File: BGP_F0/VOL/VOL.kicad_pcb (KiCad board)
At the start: 2 copper layers, 20 x 26 mm, 2 parts, among them J1 Conn_01x03

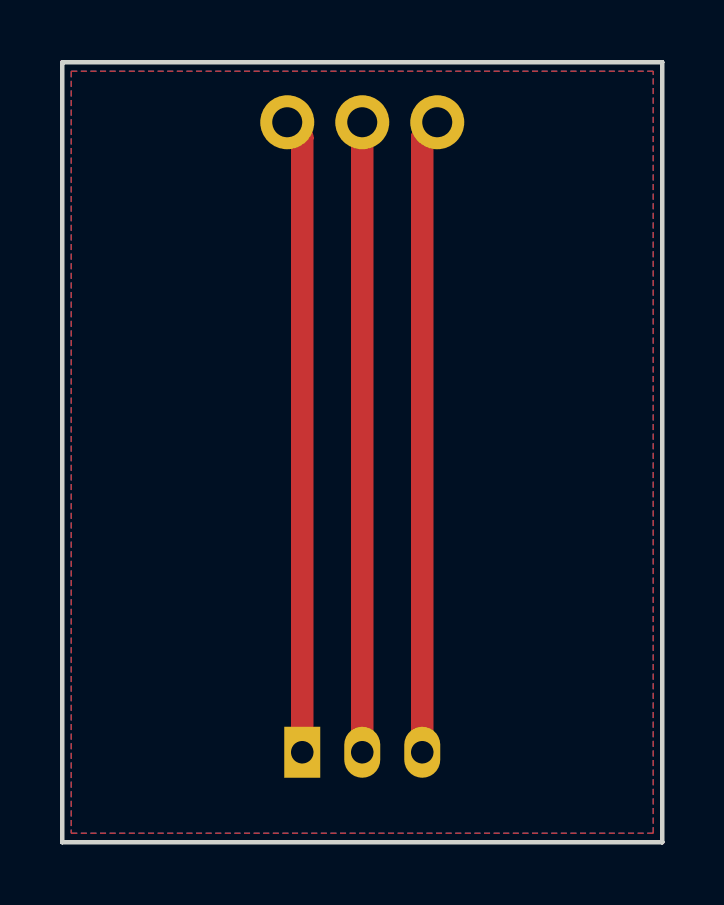
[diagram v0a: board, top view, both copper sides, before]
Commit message: Removed old boards, all F0 are now 26mm deep
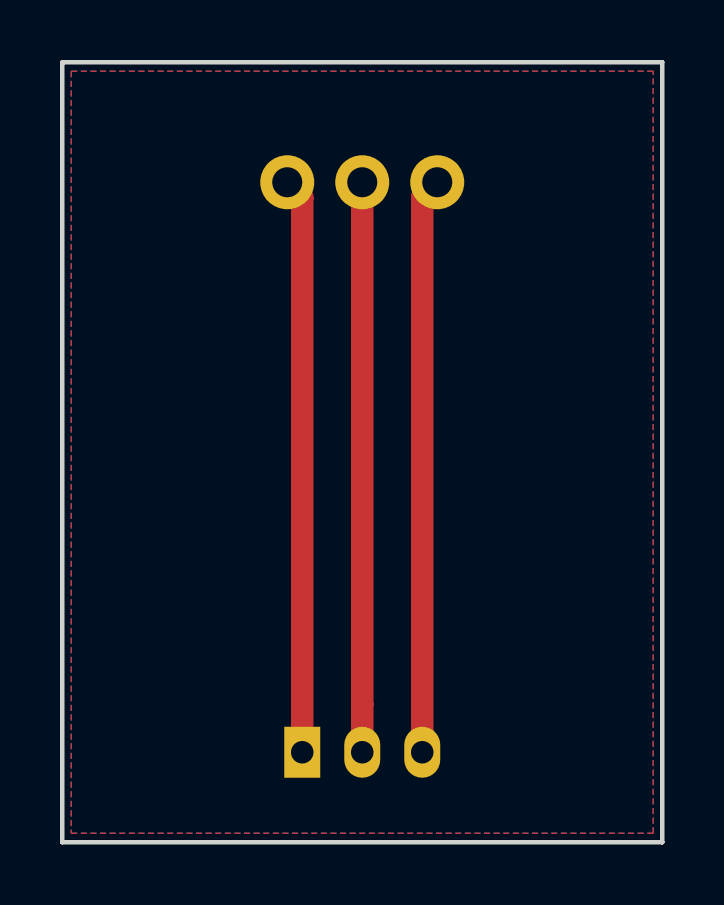
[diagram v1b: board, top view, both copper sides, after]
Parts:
- moved RV1 2.00 mm to (145.5, 80.0)
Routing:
- net /VOL_3: track 21.2 -> 19.2 mm
- net /VOL_2: track 21.0 -> 19.0 mm
- net /VOL_1: track 21.2 -> 19.2 mm
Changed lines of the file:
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@@
-(kicad_pcb (version 4) (host pcbnew 4.0.7)
+(kicad_pcb (version 4) (host pcbnew 4.0.4-1.fc24-product)
   (general
     (links 3)
     (no_connects 0)
-    (area 137.924999 75.924999 158.075001 102.075001)
+    (area 137.924999 75.424999 158.075001 102.075001)
     (thickness 1.6)
     (drawings 8)
-    (tracks 5)
+    (tracks 6)
     (zones 0)
     (modules 2)
@@
     (add_net /VOL_3)
   )
+  (module LIBS:Potentiometer_Alps_RK097_Single_Vertical (layer B.Cu)
+    (at 145.5 80 90)
+    (descr "Potentiometer, vertically mounted, Omeg PC16PU, Omeg PC16PU, Omeg PC16PU, Vishay/Spectrol 248GJ/249GJ Single, Vishay/Spectrol 248GJ/249GJ Single, Vishay/Spectrol 248GJ/249GJ Single, Vishay/Spectrol 248GH/249GH Single, Vishay/Spectrol 148/149 Single, Vishay/Spectrol 148/149 Single, Vishay/Spectrol 148/149 Single, Vishay/Spectrol 148A/149A Single with mounting plates, Vishay/Spectrol 148/149 Double, Vishay/Spectrol 148A/149A Double with mounting plates, Piher PC-16 Single, Piher PC-16 Single, Piher PC-16 Single, Piher PC-16SV Single, Piher PC-16 Double, Piher PC-16 Triple, Piher T16H Single, Piher T16L Single, Piher T16H Double, Alps RK163 Single, Alps RK163 Double, Alps RK097 Single, http://www.alps.com/prod/info/E/HTML/Potentiometer/RotaryPotentiometers/RK097/RK097111080J.html")
+    (tags "Potentiometer vertical  Omeg PC16PU  Omeg PC16PU  Omeg PC16PU  Vishay/Spectrol 248GJ/249GJ Single  Vishay/Spectrol 248GJ/249GJ Single  Vishay/Spectrol 248GJ/249GJ Single  Vishay/Spectrol 248GH/249GH Single  Vishay/Spectrol 148/149 Single  Vishay/Spectrol 148/149 Single  Vishay/Spectrol 148/149 Single  Vishay/Spectrol 148A/149A Single with mounting plates  Vishay/Spectrol 148/149 Double  Vishay/Spectrol 148A/149A Double with mounting plates  Piher PC-16 Single  Piher PC-16 Single  Piher PC-16 Single  Piher PC-16SV Single  Piher PC-16 Double  Piher PC-16 Triple  Piher T16H Single  Piher T16L Single  Piher T16H Double  Alps RK163 Single  Alps RK163 Double  Alps RK097 Single")
+    (fp_text reference RV1 (at 0 7.9 90) (layer B.SilkS)
+      (effects (font (size 0.6 0.6) (thickness 0.15)) (justify mirror))
+    )
+    (fp_text value POT (at 0 -3.5 90) (layer B.Fab) hide
+      (effects (font (size 0.6 0.6) (thickness 0.15)) (justify mirror))
+    )
+    (fp_line (start -2.05 7.25) (end -2.05 -2.25) (layer B.Fab) (width 0.1))
+    (fp_line (start -2.05 -2.25) (end 2 -2.25) (layer B.Fab) (width 0.1))
+    (fp_line (start 2 -2.25) (end 2 7.25) (layer B.Fab) (width 0.1))
+    (fp_line (start 2 7.25) (end -2.05 7.25) (layer B.Fab) (width 0.1))
+    (fp_line (start -2.11 7.31) (end 2.06 7.31) (layer B.SilkS) (width 0.12))
+    (fp_line (start -2.11 -2.31) (end 2.06 -2.31) (layer B.SilkS) (width 0.12))
+    (fp_line (start -2.11 7.31) (end -2.11 -2.31) (layer B.SilkS) (width 0.12))
+    (fp_line (start 2.06 7.31) (end 2.06 -2.31) (layer B.SilkS) (width 0.12))
+    (fp_line (start -2.3 7.5) (end -2.3 -2.5) (layer B.CrtYd) (width 0.05))
+    (fp_line (start -2.3 -2.5) (end 2.25 -2.5) (layer B.CrtYd) (width 0.05))
+    (fp_line (start 2.25 -2.5) (end 2.25 7.5) (layer B.CrtYd) (width 0.05))
+    (fp_line (start 2.25 7.5) (end -2.3 7.5) (layer B.CrtYd) (width 0.05))
+    (pad 3 thru_hole circle (at 0 5 90) (size 1.8 1.8) (drill 1) (layers *.Cu *.Mask)
+      (net 3 /VOL_3))
+    (pad 2 thru_hole circle (at 0 2.5 90) (size 1.8 1.8) (drill 1) (layers *.Cu *.Mask)
+      (net 2 /VOL_2))
+    (pad 1 thru_hole circle (at 0 0 90) (size 1.8 1.8) (drill 1) (layers *.Cu *.Mask)
+      (net 1 /VOL_1))
+    (model Potentiometers.3dshapes/Potentiometer_Alps_RK097_Single_Vertical.wrl
+      (at (xyz 0 0 0))
+      (scale (xyz 0.393701 0.393701 0.393701))
+      (rotate (xyz 0 0 0))
+    )
+  )
   (module Connectors_JST:JST_PH_B3B-PH-K_03x2.00mm_Straight (layer B.Cu)
     (at 146 99)
@@
     )
   )
-  (module LIBS:Potentiometer_Alps_RK097_Single_Vertical (layer B.Cu)
-    (at 145.5 78 90)
-    (descr "Potentiometer, vertically mounted, Omeg PC16PU, Omeg PC16PU, Omeg PC16PU, Vishay/Spectrol 248GJ/249GJ Single, Vishay/Spectrol 248GJ/249GJ Single, Vishay/Spectrol 248GJ/249GJ Single, Vishay/Spectrol 248GH/249GH Single, Vishay/Spectrol 148/149 Single, Vishay/Spectrol 148/149 Single, Vishay/Spectrol 148/149 Single, Vishay/Spectrol 148A/149A Single with mounting plates, Vishay/Spectrol 148/149 Double, Vishay/Spectrol 148A/149A Double with mounting plates, Piher PC-16 Single, Piher PC-16 Single, Piher PC-16 Single, Piher PC-16SV Single, Piher PC-16 Double, Piher PC-16 Triple, Piher T16H Single, Piher T16L Single, Piher T16H Double, Alps RK163 Single, Alps RK163 Double, Alps RK097 Single, http://www.alps.com/prod/info/E/HTML/Potentiometer/RotaryPotentiometers/RK097/RK097111080J.html")
-    (tags "Potentiometer vertical  Omeg PC16PU  Omeg PC16PU  Omeg PC16PU  Vishay/Spectrol 248GJ/249GJ Single  Vishay/Spectrol 248GJ/249GJ Single  Vishay/Spectrol 248GJ/249GJ Single  Vishay/Spectrol 248GH/249GH Single  Vishay/Spectrol 148/149 Single  Vishay/Spectrol 148/149 Single  Vishay/Spectrol 148/149 Single  Vishay/Spectrol 148A/149A Single with mounting plates  Vishay/Spectrol 148/149 Double  Vishay/Spectrol 148A/149A Double with mounting plates  Piher PC-16 Single  Piher PC-16 Single  Piher PC-16 Single  Piher PC-16SV Single  Piher PC-16 Double  Piher PC-16 Triple  Piher T16H Single  Piher T16L Single  Piher T16H Double  Alps RK163 Single  Alps RK163 Double  Alps RK097 Single")
-    (fp_text reference RV1 (at 0 7.9 90) (layer B.SilkS)
-      (effects (font (size 0.6 0.6) (thickness 0.15)) (justify mirror))
-    )
-    (fp_text value POT (at 0 -3.5 90) (layer B.Fab) hide
-      (effects (font (size 0.6 0.6) (thickness 0.15)) (justify mirror))
-    )
-    (fp_line (start -2.05 7.25) (end -2.05 -2.25) (layer B.Fab) (width 0.1))
-    (fp_line (start -2.05 -2.25) (end 2 -2.25) (layer B.Fab) (width 0.1))
-    (fp_line (start 2 -2.25) (end 2 7.25) (layer B.Fab) (width 0.1))
-    (fp_line (start 2 7.25) (end -2.05 7.25) (layer B.Fab) (width 0.1))
-    (fp_line (start -2.11 7.31) (end 2.06 7.31) (layer B.SilkS) (width 0.12))
-    (fp_line (start -2.11 -2.31) (end 2.06 -2.31) (layer B.SilkS) (width 0.12))
-    (fp_line (start -2.11 7.31) (end -2.11 -2.31) (layer B.SilkS) (width 0.12))
-    (fp_line (start 2.06 7.31) (end 2.06 -2.31) (layer B.SilkS) (width 0.12))
-    (fp_line (start -2.3 7.5) (end -2.3 -2.5) (layer B.CrtYd) (width 0.05))
-    (fp_line (start -2.3 -2.5) (end 2.25 -2.5) (layer B.CrtYd) (width 0.05))
-    (fp_line (start 2.25 -2.5) (end 2.25 7.5) (layer B.CrtYd) (width 0.05))
-    (fp_line (start 2.25 7.5) (end -2.3 7.5) (layer B.CrtYd) (width 0.05))
-    (pad 3 thru_hole circle (at 0 5 90) (size 1.8 1.8) (drill 1) (layers *.Cu *.Mask)
-      (net 3 /VOL_3))
-    (pad 2 thru_hole circle (at 0 2.5 90) (size 1.8 1.8) (drill 1) (layers *.Cu *.Mask)
-      (net 2 /VOL_2))
-    (pad 1 thru_hole circle (at 0 0 90) (size 1.8 1.8) (drill 1) (layers *.Cu *.Mask)
-      (net 1 /VOL_1))
-    (model Potentiometers.3dshapes/Potentiometer_Alps_RK097_Single_Vertical.wrl
-      (at (xyz 0 0 0))
-      (scale (xyz 0.393701 0.393701 0.393701))
-      (rotate (xyz 0 0 0))
-    )
-  )
   (gr_line (start 157.7 101.7) (end 157.7 76.3) (layer Margin) (width 0.2))
   (gr_line (start 138.3 101.7) (end 157.7 101.7) (layer Margin) (width 0.2))
@@
   (gr_line (start 138 76) (end 138 102) (layer Edge.Cuts) (width 0.15))
   (gr_line (start 158 76) (end 138 76) (layer Edge.Cuts) (width 0.15))
-  (segment (start 146 99) (end 146 78.5) (width 0.75) (layer F.Cu) (net 1))
-  (segment (start 146 78.5) (end 145.5 78) (width 0.75) (layer F.Cu) (net 1))
-  (segment (start 148 99) (end 148 78) (width 0.75) (layer F.Cu) (net 2))
-  (segment (start 150 99) (end 150 78.5) (width 0.75) (layer F.Cu) (net 3))
-  (segment (start 150 78.5) (end 150.5 78) (width 0.75) (layer F.Cu) (net 3))
+  (segment (start 146 99) (end 146 80.5) (width 0.75) (layer F.Cu) (net 1))
+  (segment (start 146 80.5) (end 145.5 80) (width 0.75) (layer F.Cu) (net 1))
+  (segment (start 148 99) (end 148 97.4) (width 0.75) (layer F.Cu) (net 2))
+  (segment (start 148 97.4) (end 148 80) (width 0.75) (layer F.Cu) (net 2))
+  (segment (start 150 99) (end 150 80.5) (width 0.75) (layer F.Cu) (net 3))
+  (segment (start 150 80.5) (end 150.5 80) (width 0.75) (layer F.Cu) (net 3))
   (zone (net 0) (net_name "") (layer B.Cu) (hatch edge 0.508)
     (connect_pads (clearance 0.3))

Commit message: F0 Final
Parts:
- removed J1: Conn_01x03, Connectors_JST:JST_PH_B3B-PH-K_03x2.00mm_Straight
- added C1: 47n, Capacitors_SMD:C_1206, F.Cu at (150.6, 89.1)
- added P1: CONN_01X02, Connectors_JST:JST_PH_B2B-PH-K_02x2.00mm_Straight, B.Cu at (147.0, 98.5)
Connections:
- RV1 pad 2: /VOL_2 -> /VOL_1
- RV1 pad 3: /VOL_3 -> Net-(C1-Pad1)
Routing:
- net /VOL_2: track 19.0 -> 0.00 mm
- net /VOL_3: track 19.2 -> 8.56 mm
- net Net-(C1-Pad1): track 0.00 -> 8.35 mm
- net /VOL_1: track 19.2 -> 21.6 mm
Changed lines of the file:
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@@
 (kicad_pcb (version 4) (host pcbnew 4.0.4-1.fc24-product)
   (general
-    (links 3)
-    (no_connects 0)
-    (area 137.924999 75.424999 158.075001 102.075001)
+    (links 4)
+    (no_connects 3)
+    (area 137.924999 75.924999 158.075001 102.075001)
     (thickness 1.6)
     (drawings 8)
-    (tracks 6)
+    (tracks 12)
     (zones 0)
-    (modules 2)
+    (modules 3)
     (nets 4)
   )
@@
   (net 0 "")
   (net 1 /VOL_1)
-  (net 2 /VOL_2)
-  (net 3 /VOL_3)
+  (net 2 /VOL_3)
+  (net 3 "Net-(C1-Pad1)")
   (net_class Default "This is the default net class."
     (clearance 0.3)
@@
     (uvia_drill 0.1)
     (add_net /VOL_1)
-    (add_net /VOL_2)
     (add_net /VOL_3)
+    (add_net "Net-(C1-Pad1)")
   )
   (module LIBS:Potentiometer_Alps_RK097_Single_Vertical (layer B.Cu)
@@
     (fp_line (start 2.25 7.5) (end -2.3 7.5) (layer B.CrtYd) (width 0.05))
     (pad 3 thru_hole circle (at 0 5 90) (size 1.8 1.8) (drill 1) (layers *.Cu *.Mask)
-      (net 3 /VOL_3))
+      (net 3 "Net-(C1-Pad1)"))
     (pad 2 thru_hole circle (at 0 2.5 90) (size 1.8 1.8) (drill 1) (layers *.Cu *.Mask)
-      (net 2 /VOL_2))
+      (net 1 /VOL_1))
     (pad 1 thru_hole circle (at 0 0 90) (size 1.8 1.8) (drill 1) (layers *.Cu *.Mask)
       (net 1 /VOL_1))
@@
     )
   )
-  (module Connectors_JST:JST_PH_B3B-PH-K_03x2.00mm_Straight (layer B.Cu)
-    (at 146 99)
-    (descr "JST PH series connector, B3B-PH-K, top entry type, through hole, Datasheet: http://www.jst-mfg.com/product/pdf/eng/ePH.pdf")
+  (module Capacitors_SMD:C_1206 (layer F.Cu)
+    (at 150.6 89.1 270)
+    (descr "Capacitor SMD 1206, reflow soldering, AVX (see smccp.pdf)")
+    (tags "capacitor 1206")
+    (attr smd)
+    (fp_text reference C1 (at 0 -2.3 270) (layer F.SilkS)
+      (effects (font (size 0.6 0.6) (thickness 0.15)))
+    )
+    (fp_text value 47n (at 0 2.3 270) (layer F.Fab)
+      (effects (font (size 0.6 0.6) (thickness 0.15)))
+    )
+    (fp_line (start -2.3 -1.15) (end 2.3 -1.15) (layer F.CrtYd) (width 0.05))
+    (fp_line (start -2.3 1.15) (end 2.3 1.15) (layer F.CrtYd) (width 0.05))
+    (fp_line (start -2.3 -1.15) (end -2.3 1.15) (layer F.CrtYd) (width 0.05))
+    (fp_line (start 2.3 -1.15) (end 2.3 1.15) (layer F.CrtYd) (width 0.05))
+    (fp_line (start 1 -1.025) (end -1 -1.025) (layer F.SilkS) (width 0.15))
+    (fp_line (start -1 1.025) (end 1 1.025) (layer F.SilkS) (width 0.15))
+    (pad 1 smd rect (at -1.5 0 270) (size 1 1.6) (layers F.Cu F.Paste F.Mask)
+      (net 3 "Net-(C1-Pad1)"))
+    (pad 2 smd rect (at 1.5 0 270) (size 1 1.6) (layers F.Cu F.Paste F.Mask)
+      (net 2 /VOL_3))
+    (model Capacitors_SMD.3dshapes/C_1206.wrl
+      (at (xyz 0 0 0))
+      (scale (xyz 1 1 1))
+      (rotate (xyz 0 0 0))
+    )
+  )
+  (module Connectors_JST:JST_PH_B2B-PH-K_02x2.00mm_Straight (layer B.Cu)
+    (at 147 98.5)
+    (descr "JST PH series connector, B2B-PH-K, top entry type, through hole, Datasheet: http://www.jst-mfg.com/product/pdf/eng/ePH.pdf")
     (tags "connector jst ph")
-    (fp_text reference J1 (at 5.6 -3.4) (layer B.SilkS)
-      (effects (font (size 0.6 0.6) (thickness 0.15)) (justify mirror))
-    )
-    (fp_text value Conn_01x03 (at 2 -3.8) (layer B.Fab) hide
+    (fp_text reference P1 (at 3.5 -3.6) (layer B.SilkS)
+      (effects (font (size 0.6 0.6) (thickness 0.15)) (justify mirror))
+    )
+    (fp_text value CONN_01X02 (at 1 -3.8) (layer B.Fab) hide
       (effects (font (size 0.6 0.6) (thickness 0.15)) (justify mirror))
     )
     (fp_line (start -2.05 1.8) (end -2.05 -2.9) (layer B.SilkS) (width 0.12))
-    (fp_line (start -2.05 -2.9) (end 6.05 -2.9) (layer B.SilkS) (width 0.12))
-    (fp_line (start 6.05 -2.9) (end 6.05 1.8) (layer B.SilkS) (width 0.12))
-    (fp_line (start 6.05 1.8) (end -2.05 1.8) (layer B.SilkS) (width 0.12))
+    (fp_line (start -2.05 -2.9) (end 4.05 -2.9) (layer B.SilkS) (width 0.12))
+    (fp_line (start 4.05 -2.9) (end 4.05 1.8) (layer B.SilkS) (width 0.12))
+    (fp_line (start 4.05 1.8) (end -2.05 1.8) (layer B.SilkS) (width 0.12))
     (fp_line (start 0.5 1.8) (end 0.5 1.2) (layer B.SilkS) (width 0.12))
     (fp_line (start 0.5 1.2) (end -1.45 1.2) (layer B.SilkS) (width 0.12))
     (fp_line (start -1.45 1.2) (end -1.45 -2.3) (layer B.SilkS) (width 0.12))
-    (fp_line (start -1.45 -2.3) (end 5.45 -2.3) (layer B.SilkS) (width 0.12))
-    (fp_line (start 5.45 -2.3) (end 5.45 1.2) (layer B.SilkS) (width 0.12))
-    (fp_line (start 5.45 1.2) (end 3.5 1.2) (layer B.SilkS) (width 0.12))
-    (fp_line (start 3.5 1.2) (end 3.5 1.8) (layer B.SilkS) (width 0.12))
+    (fp_line (start -1.45 -2.3) (end 3.45 -2.3) (layer B.SilkS) (width 0.12))
+    (fp_line (start 3.45 -2.3) (end 3.45 1.2) (layer B.SilkS) (width 0.12))
+    (fp_line (start 3.45 1.2) (end 1.5 1.2) (layer B.SilkS) (width 0.12))
+    (fp_line (start 1.5 1.2) (end 1.5 1.8) (layer B.SilkS) (width 0.12))
     (fp_line (start -2.05 0.5) (end -1.45 0.5) (layer B.SilkS) (width 0.12))
     (fp_line (start -2.05 -0.8) (end -1.45 -0.8) (layer B.SilkS) (width 0.12))
-    (fp_line (start 6.05 0.5) (end 5.45 0.5) (layer B.SilkS) (width 0.12))
-    (fp_line (start 6.05 -0.8) (end 5.45 -0.8) (layer B.SilkS) (width 0.12))
+    (fp_line (start 4.05 0.5) (end 3.45 0.5) (layer B.SilkS) (width 0.12))
+    (fp_line (start 4.05 -0.8) (end 3.45 -0.8) (layer B.SilkS) (width 0.12))
     (fp_line (start -0.3 1.8) (end -0.3 2) (layer B.SilkS) (width 0.12))
     (fp_line (start -0.3 2) (end -0.6 2) (layer B.SilkS) (width 0.12))
@@
     (fp_line (start 1.1 -1.8) (end 1.1 -2.3) (layer B.SilkS) (width 0.12))
     (fp_line (start 1 -2.3) (end 1 -1.8) (layer B.SilkS) (width 0.12))
-    (fp_line (start 2.9 -2.3) (end 2.9 -1.8) (layer B.SilkS) (width 0.12))
-    (fp_line (start 2.9 -1.8) (end 3.1 -1.8) (layer B.SilkS) (width 0.12))
-    (fp_line (start 3.1 -1.8) (end 3.1 -2.3) (layer B.SilkS) (width 0.12))
-    (fp_line (start 3 -2.3) (end 3 -1.8) (layer B.SilkS) (width 0.12))
     (fp_line (start -1.1 2.1) (end -2.35 2.1) (layer B.SilkS) (width 0.12))
     (fp_line (start -2.35 2.1) (end -2.35 0.85) (layer B.SilkS) (width 0.12))
@@
     (fp_line (start -2.35 2.1) (end -2.35 0.85) (layer B.Fab) (width 0.1))
     (fp_line (start -1.95 1.7) (end -1.95 -2.8) (layer B.Fab) (width 0.1))
-    (fp_line (start -1.95 -2.8) (end 5.95 -2.8) (layer B.Fab) (width 0.1))
-    (fp_line (start 5.95 -2.8) (end 5.95 1.7) (layer B.Fab) (width 0.1))
-    (fp_line (start 5.95 1.7) (end -1.95 1.7) (layer B.Fab) (width 0.1))
+    (fp_line (start -1.95 -2.8) (end 3.95 -2.8) (layer B.Fab) (width 0.1))
+    (fp_line (start 3.95 -2.8) (end 3.95 1.7) (layer B.Fab) (width 0.1))
+    (fp_line (start 3.95 1.7) (end -1.95 1.7) (layer B.Fab) (width 0.1))
     (fp_line (start -2.45 2.2) (end -2.45 -3.3) (layer B.CrtYd) (width 0.05))
-    (fp_line (start -2.45 -3.3) (end 6.45 -3.3) (layer B.CrtYd) (width 0.05))
-    (fp_line (start 6.45 -3.3) (end 6.45 2.2) (layer B.CrtYd) (width 0.05))
-    (fp_line (start 6.45 2.2) (end -2.45 2.2) (layer B.CrtYd) (width 0.05))
-    (fp_text user %R (at 2 -1.5) (layer B.Fab) hide
-      (effects (font (size 1 1) (thickness 0.15)) (justify mirror))
+    (fp_line (start -2.45 -3.3) (end 4.45 -3.3) (layer B.CrtYd) (width 0.05))
+    (fp_line (start 4.45 -3.3) (end 4.45 2.2) (layer B.CrtYd) (width 0.05))
+    (fp_line (start 4.45 2.2) (end -2.45 2.2) (layer B.CrtYd) (width 0.05))
+    (fp_text user %R (at 1 -1.5) (layer B.Fab) hide
+      (effects (font (size 0.6 0.6) (thickness 0.15)) (justify mirror))
     )
     (pad 1 thru_hole rect (at 0 0) (size 1.2 1.7) (drill 0.75) (layers *.Cu *.Mask)
       (net 1 /VOL_1))
     (pad 2 thru_hole oval (at 2 0) (size 1.2 1.7) (drill 0.75) (layers *.Cu *.Mask)
-      (net 2 /VOL_2))
-    (pad 3 thru_hole oval (at 4 0) (size 1.2 1.7) (drill 0.75) (layers *.Cu *.Mask)
-      (net 3 /VOL_3))
-    (model ${KISYS3DMOD}/Connectors_JST.3dshapes/JST_PH_B3B-PH-K_03x2.00mm_Straight.wrl
+      (net 2 /VOL_3))
+    (model ${KISYS3DMOD}/Connectors_JST.3dshapes/JST_PH_B2B-PH-K_02x2.00mm_Straight.wrl
       (at (xyz 0 0 0))
       (scale (xyz 1 1 1))
@@
   (gr_line (start 138 76) (end 138 102) (layer Edge.Cuts) (width 0.15))
   (gr_line (start 158 76) (end 138 76) (layer Edge.Cuts) (width 0.15))
-  (segment (start 146 99) (end 146 80.5) (width 0.75) (layer F.Cu) (net 1))
+  (segment (start 146.7 81.2) (end 146.8 81.2) (width 0.75) (layer F.Cu) (net 1))
+  (segment (start 146.8 81.2) (end 148 80) (width 0.75) (layer F.Cu) (net 1))
+  (segment (start 147 98.5) (end 146.7 98.2) (width 0.75) (layer F.Cu) (net 1))
+  (segment (start 146.7 98.2) (end 146.7 81.2) (width 0.75) (layer F.Cu) (net 1))
+  (segment (start 146.7 81.2) (end 145.5 80) (width 0.75) (layer F.Cu) (net 1))
   (segment (start 146 80.5) (end 145.5 80) (width 0.75) (layer F.Cu) (net 1))
-  (segment (start 148 99) (end 148 97.4) (width 0.75) (layer F.Cu) (net 2))
-  (segment (start 148 97.4) (end 148 80) (width 0.75) (layer F.Cu) (net 2))
-  (segment (start 150 99) (end 150 80.5) (width 0.75) (layer F.Cu) (net 3))
+  (segment (start 149 98.5) (end 150.6 96.9) (width 0.75) (layer F.Cu) (net 2))
+  (segment (start 150.6 91.85) (end 150.6 90.6) (width 0.75) (layer F.Cu) (net 2))
+  (segment (start 150.6 96.9) (end 150.6 91.85) (width 0.75) (layer F.Cu) (net 2))
+  (segment (start 150.5 80) (end 150.5 87.5) (width 0.75) (layer F.Cu) (net 3))
+  (segment (start 150.5 87.5) (end 150.6 87.6) (width 0.75) (layer F.Cu) (net 3))
   (segment (start 150 80.5) (end 150.5 80) (width 0.75) (layer F.Cu) (net 3))
   (zone (net 0) (net_name "") (layer B.Cu) (hatch edge 0.508)
